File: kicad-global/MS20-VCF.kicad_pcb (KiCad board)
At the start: 2 copper layers, 118 x 128.5 mm, 59 parts, among them J5 Power Input, J6 FilterCV1, J7 FilterIn1, J8 FilterOut1, Q1 BC559, Q2 BC559, SW1 Hpass/Lpass Switch, U1 LM13700, U2 TL072

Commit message: update to v1.2 on silkscreen
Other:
- board text added: "MS-20 VCF Face plate V1.2 BleepSound 2023"
- board text added: "MS-20 VCF V1.2 BleepSound 2023"
- board text removed: "MS-20 VCF Face plate V1.1 BleepSound 2022"
- board text removed: "MS-20 VCF V1.1 BleepSound 2022"
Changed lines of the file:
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@@
   (gr_line (start 149.55 127.1) (end 150.4 127.1) (layer "F.SilkS") (width 0.12))
   (gr_line (start 327.55 34.25) (end 328.05 36.15) (layer "F.SilkS") (width 0.12))
-  (gr_arc (start 332.769006 50.73996) (mid 324.729991 49.155782) (end 327.954039 41.623126) (layer "F.SilkS") (width 0.12))
+  (gr_arc (start 332.769006 50.73996) (mid 324.72999 49.155782) (end 327.954039 41.623126) (layer "F.SilkS") (width 0.12))
   (gr_line (start 314.75 14.05) (end 313.75 14.05) (layer "F.SilkS") (width 0.12))
   (gr_line (start 376.25 19.05) (end 376.65 19.65) (layer "F.SilkS") (width 0.12))
@@
     (effects (font (size 1.5 1.5) (thickness 0.3)) (justify mirror))
   )
-  (gr_text "MS-20 VCF\nFace plate\nV1.1 BleepSound\n2022" (at 128 31) (layer "B.SilkS")
+  (gr_text "MS-20 VCF\nFace plate\nV1.2 BleepSound\n2023" (at 128 31) (layer "B.SilkS")
     (effects (font (size 1 1) (thickness 0.15)) (justify mirror))
   )
-  (gr_text "MS-20 VCF\nV1.1 BleepSound\n2022" (at 42 39.5) (layer "F.SilkS")
+  (gr_text "MS-20 VCF\nV1.2 BleepSound\n2023" (at 42 39.5) (layer "F.SilkS")
     (effects (font (size 1 1) (thickness 0.15)))
   )

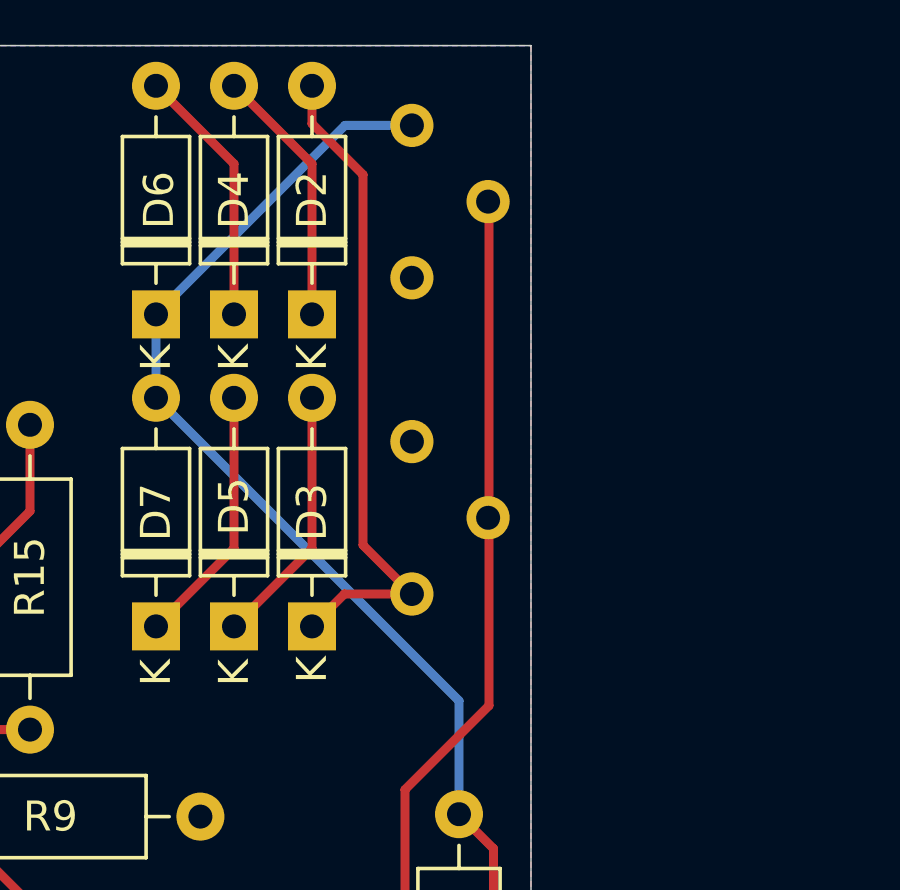
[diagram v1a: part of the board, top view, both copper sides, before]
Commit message: update footprint for trimmer
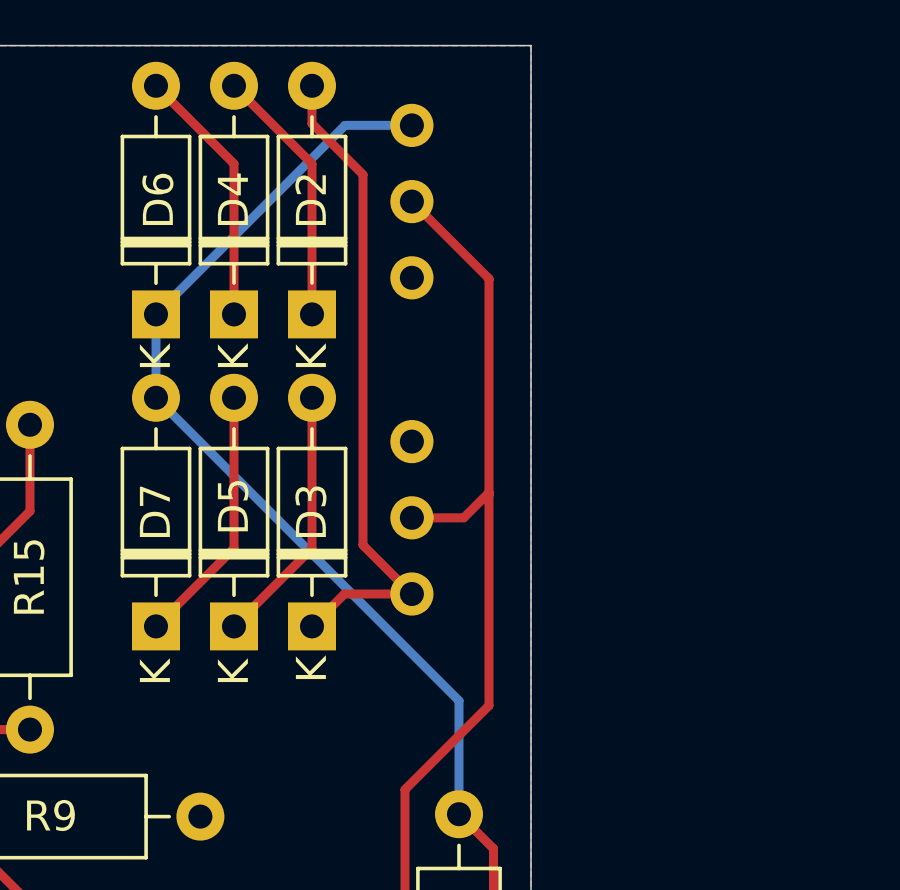
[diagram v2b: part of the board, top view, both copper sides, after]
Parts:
- ResLv1, ResVol1: footprint Potentiometer_THT:Potentiometer_Bourns_3386X_Horizontal -> Potentiometer_THT:Potentiometer_Bourns_3386C_Horizontal
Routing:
- net Net-(C1-Pad2): track 84.5 -> 88.5 mm

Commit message: update repo organization
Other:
- board text added: "10HP"
- board text removed: "12HP"
